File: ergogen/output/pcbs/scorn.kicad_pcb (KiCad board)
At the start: 2 copper layers, 150.5 x 92.9 mm, 46 parts

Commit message: pcb layout complete
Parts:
- removed B1: , E73:SW_TACT_ALPS_SKQGABE010
- removed OLED1: OLED, lib:OLED_headers
- removed S1, S10, S11, S12, S13, S14, S15, S16, S17, S18, S19, S2, S20, S21, S3, S4, S5, S6, S7, S8, S9: , PG1350
- added D22: , ceoloide:diode_tht_sod123, B.Cu at (141.0, 149.8)
- added D23: , ceoloide:diode_tht_sod123, B.Cu at (137.6, 133.1)
- added D24: , ceoloide:diode_tht_sod123, B.Cu at (134.3, 116.4)
- added D25: , ceoloide:diode_tht_sod123, B.Cu at (159.3, 146.6)
- added D26: , ceoloide:diode_tht_sod123, B.Cu at (157.7, 129.7)
- added D27: , ceoloide:diode_tht_sod123, B.Cu at (156.0, 112.7)
- added D28: , ceoloide:diode_tht_sod123, B.Cu at (177.1, 133.3)
- added D29: , ceoloide:diode_tht_sod123, B.Cu at (177.1, 116.3)
- added D30: , ceoloide:diode_tht_sod123, B.Cu at (177.1, 99.3)
- added D31: , ceoloide:diode_tht_sod123, B.Cu at (195.1, 128.3)
- added D32: , ceoloide:diode_tht_sod123, B.Cu at (195.1, 111.3)
- added D33: , ceoloide:diode_tht_sod123, B.Cu at (195.1, 94.3)
- added D34: , ceoloide:diode_tht_sod123, B.Cu at (213.1, 133.3)
- added D35: , ceoloide:diode_tht_sod123, B.Cu at (213.1, 116.3)
- added D36: , ceoloide:diode_tht_sod123, B.Cu at (213.1, 99.3)
- added D37: , ceoloide:diode_tht_sod123, B.Cu at (231.1, 135.3)
- added D38: , ceoloide:diode_tht_sod123, B.Cu at (231.1, 118.3)
- added D39: , ceoloide:diode_tht_sod123, B.Cu at (231.1, 101.3)
- added D40: , ceoloide:diode_tht_sod123, B.Cu at (210.0, 159.5)
- added D41: , ceoloide:diode_tht_sod123, B.Cu at (233.2, 158.1)
- added D42: , ceoloide:diode_tht_sod123, B.Cu at (256.9, 161.4)
- added DISP1: , ceoloide:display_ssd1306, F.Cu at (270.0, 114.8)
- added LED1: , ceoloide:led_SK6812mini-e (per-key, reversible), B.Cu at (148.4, 145.5)
- added LED10: , ceoloide:led_SK6812mini-e (per-key, reversible), B.Cu at (203.0, 125.1)
- added LED11: , ceoloide:led_SK6812mini-e (per-key, reversible), B.Cu at (203.0, 108.1)
- added LED12: , ceoloide:led_SK6812mini-e (per-key, reversible), B.Cu at (203.0, 91.1)
- added LED13: , ceoloide:led_SK6812mini-e (per-key, reversible), B.Cu at (221.0, 130.1)
- added LED14: , ceoloide:led_SK6812mini-e (per-key, reversible), B.Cu at (221.0, 113.1)
- added LED15: , ceoloide:led_SK6812mini-e (per-key, reversible), B.Cu at (221.0, 96.1)
- added LED16: , ceoloide:led_SK6812mini-e (per-key, reversible), B.Cu at (239.0, 132.1)
- added LED17: , ceoloide:led_SK6812mini-e (per-key, reversible), B.Cu at (239.0, 115.1)
- added LED18: , ceoloide:led_SK6812mini-e (per-key, reversible), B.Cu at (239.0, 98.1)
- added LED19: , ceoloide:led_SK6812mini-e (per-key, reversible), B.Cu at (217.6, 155.6)
- added LED2: , ceoloide:led_SK6812mini-e (per-key, reversible), B.Cu at (145.0, 128.8)
- added LED20: , ceoloide:led_SK6812mini-e (per-key, reversible), B.Cu at (241.4, 155.6)
- added LED21: , ceoloide:led_SK6812mini-e (per-key, reversible), B.Cu at (265.4, 160.8)
- added LED3: , ceoloide:led_SK6812mini-e (per-key, reversible), B.Cu at (141.6, 112.1)
- added LED4: , ceoloide:led_SK6812mini-e (per-key, reversible), B.Cu at (167.0, 142.8)
- added LED5: , ceoloide:led_SK6812mini-e (per-key, reversible), B.Cu at (165.3, 125.9)
- added LED6: , ceoloide:led_SK6812mini-e (per-key, reversible), B.Cu at (163.6, 109.0)
- added LED7: , ceoloide:led_SK6812mini-e (per-key, reversible), B.Cu at (185.0, 130.1)
- added LED8: , ceoloide:led_SK6812mini-e (per-key, reversible), B.Cu at (185.0, 113.1)
- added LED9: , ceoloide:led_SK6812mini-e (per-key, reversible), B.Cu at (185.0, 96.1)
- added MH1: , ceoloide:mounting_hole_npth, F.Cu at (154.4, 124.1)
- added MH2: , ceoloide:mounting_hole_npth, F.Cu at (157.3, 140.9)
- added MH3: , ceoloide:mounting_hole_npth, F.Cu at (255.0, 97.8)
- added MH4: , ceoloide:mounting_hole_npth, F.Cu at (275.9, 157.6)
- added MH5: , ceoloide:mounting_hole_npth, F.Cu at (203.2, 163.6)
- added RST1: , ceoloide:reset_switch_tht_top, F.Cu at (278.0, 135.8)
- added SW1: , ceoloide:switch_choc_v1_v2, B.Cu at (149.0, 150.1)
- added SW10: , ceoloide:switch_choc_v1_v2, B.Cu at (203.0, 129.8)
- added SW11: , ceoloide:switch_choc_v1_v2, B.Cu at (203.0, 112.8)
- added SW12: , ceoloide:switch_choc_v1_v2, B.Cu at (203.0, 95.8)
- added SW13: , ceoloide:switch_choc_v1_v2, B.Cu at (221.0, 134.8)
- added SW14: , ceoloide:switch_choc_v1_v2, B.Cu at (221.0, 117.8)
- added SW15: , ceoloide:switch_choc_v1_v2, B.Cu at (221.0, 100.8)
- added SW16: , ceoloide:switch_choc_v1_v2, B.Cu at (239.0, 136.8)
- added SW17: , ceoloide:switch_choc_v1_v2, B.Cu at (239.0, 119.8)
- added SW18: , ceoloide:switch_choc_v1_v2, B.Cu at (239.0, 102.8)
- added SW19: , ceoloide:switch_choc_v1_v2, B.Cu at (218.0, 160.3)
- added SW2: , ceoloide:switch_choc_v1_v2, B.Cu at (145.7, 133.4)
- added SW20: , ceoloide:switch_choc_v1_v2, B.Cu at (241.0, 160.3)
- added SW21: , ceoloide:switch_choc_v1_v2, B.Cu at (264.0, 165.3)
- added SW3: , ceoloide:switch_choc_v1_v2, B.Cu at (142.3, 116.7)
- added SW4: , ceoloide:switch_choc_v1_v2, B.Cu at (167.3, 147.5)
- added SW5: , ceoloide:switch_choc_v1_v2, B.Cu at (165.6, 130.6)
- added SW6: , ceoloide:switch_choc_v1_v2, B.Cu at (164.0, 113.7)
- added SW7: , ceoloide:switch_choc_v1_v2, B.Cu at (185.0, 134.8)
- added SW8: , ceoloide:switch_choc_v1_v2, B.Cu at (185.0, 117.8)
- added SW9: , ceoloide:switch_choc_v1_v2, B.Cu at (185.0, 100.8)
- D1, D10, D11, D12, D13, D14, D15, D16, D17, D18, D19, D2, D20, D21, D3, D4, D5, D6, D7, D8, D9: footprint ComboDiode -> ceoloide:diode_tht_sod123
- MCU1: footprint ProMicro -> ceoloide:mcu_nice_nano
- TRRS1: value TRRS-PJ-320A-dual -> (none); footprint TRRS-PJ-320A-dual -> ceoloide:trrs_pj320a (reversible, symmetric)
- moved D21 10.2 mm to (272.0, 166.3), turned to -108 degrees
- moved D4 10.2 mm to (175.1, 145.5), turned to -86 degrees
- moved D5 10.2 mm to (173.4, 128.6), turned to -86 degrees
- moved D6 10.2 mm to (171.7, 111.6), turned to -86 degrees
- moved D19 10.2 mm to (225.7, 158.1), turned to -85 degrees
- moved D10 10.2 mm to (210.9, 128.3), turned to -90 degrees
- moved D11 10.2 mm to (210.9, 111.3), turned to -90 degrees
- moved D12 10.2 mm to (210.9, 94.3), turned to -90 degrees
- moved D13 10.2 mm to (228.9, 133.3), turned to -90 degrees
- moved D14 10.2 mm to (228.9, 116.3), turned to -90 degrees
- moved D15 10.2 mm to (228.9, 99.3), turned to -90 degrees
- moved D16 10.2 mm to (246.9, 135.3), turned to -90 degrees
- moved D17 10.2 mm to (246.9, 118.3), turned to -90 degrees
- moved D18 10.2 mm to (246.9, 101.3), turned to -90 degrees
- moved D7 10.2 mm to (192.9, 133.3), turned to -90 degrees
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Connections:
- net P1 renamed MCU1_13
- net P14 renamed MCU1_10
- net P15 renamed MCU1_9
- net P18 renamed MCU1_8
- net P19 renamed MCU1_7
- net P20 renamed MCU1_6
- net P21 renamed MCU1_5
- net P4 renamed MCU1_19
- net P5 renamed MCU1_20
- net P6 renamed MCU1_21
- net P7 renamed MCU1_22
- net P8 renamed MCU1_23
- D1 pad 1: (no net) -> R2
- D10 pad 1: (no net) -> R2
- D11 pad 1: (no net) -> R1
- D12 pad 1: (no net) -> R0
- D13 pad 1: (no net) -> R2
- D14 pad 1: (no net) -> R1
- D15 pad 1: (no net) -> R0
- D16 pad 1: (no net) -> R2
- D17 pad 1: (no net) -> R1
- D18 pad 1: (no net) -> R0
- D19 pad 1: (no net) -> R3
- D2 pad 1: (no net) -> R1
- D20 pad 1: (no net) -> R3
- D21 pad 1: (no net) -> R3
- D3 pad 1: (no net) -> R0
- D4 pad 1: (no net) -> R2
- D5 pad 1: (no net) -> R1
- D6 pad 1: (no net) -> R0
- D7 pad 1: (no net) -> R2
- D8 pad 1: (no net) -> R1
- D9 pad 1: (no net) -> R0
- MCU1 pad 1: RAW -> MCU1_1
- MCU1 pad 11: P16 -> MCU1_11
- MCU1 pad 12: P10 -> MCU1_12
- MCU1 pad 14: P0 -> MCU1_14
- MCU1 pad 15: GND -> MCU1_15
- MCU1 pad 16: GND -> MCU1_16
- MCU1 pad 17: P2 -> MCU1_17
- MCU1 pad 18: P3 -> MCU1_18
- MCU1 pad 2: GND -> MCU1_2
- MCU1 pad 24: P9 -> MCU1_24
- MCU1 pad 3: RST -> MCU1_3
- MCU1 pad 4: VCC -> MCU1_4
- TRRS1 pad 3: P9 -> DAT
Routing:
- net (no net): track 0.00 -> 337.7 mm
- net VCC: track 0.00 -> 82.3 mm, vias 0 -> 21
- net GND: track 0.00 -> 82.3 mm, vias 0 -> 21
- net LED_20: track 0.00 -> 13.5 mm, vias 0 -> 2
- net LED_18: track 0.00 -> 13.5 mm, vias 0 -> 2
- net LED_16: track 0.00 -> 13.5 mm, vias 0 -> 2
- net LED_4: track 0.00 -> 13.5 mm, vias 0 -> 2
- net LED_13: track 0.00 -> 13.5 mm, vias 0 -> 2
- net LED_15: track 0.00 -> 13.5 mm, vias 0 -> 2
- net LED_14: track 0.00 -> 13.5 mm, vias 0 -> 2
- net LED_12: track 0.00 -> 13.5 mm, vias 0 -> 2
- net LED_9: track 0.00 -> 13.5 mm, vias 0 -> 2
- net LED_3: track 0.00 -> 13.5 mm, vias 0 -> 2
- net LED_2: track 0.00 -> 13.5 mm, vias 0 -> 2
- net LED_11: track 0.00 -> 13.5 mm, vias 0 -> 2
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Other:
- board text added: "JLCJLCJLCJLC"

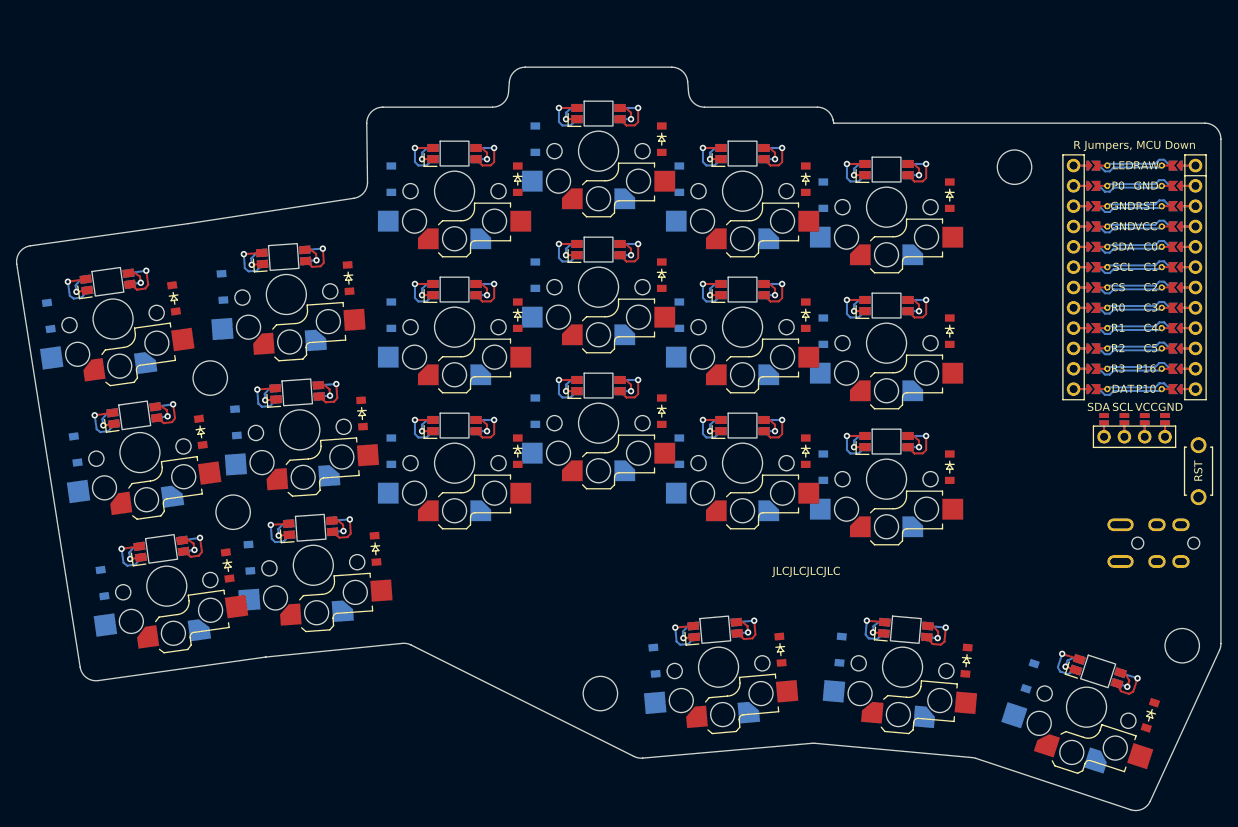
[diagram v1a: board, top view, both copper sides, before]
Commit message: stagger and splay rework
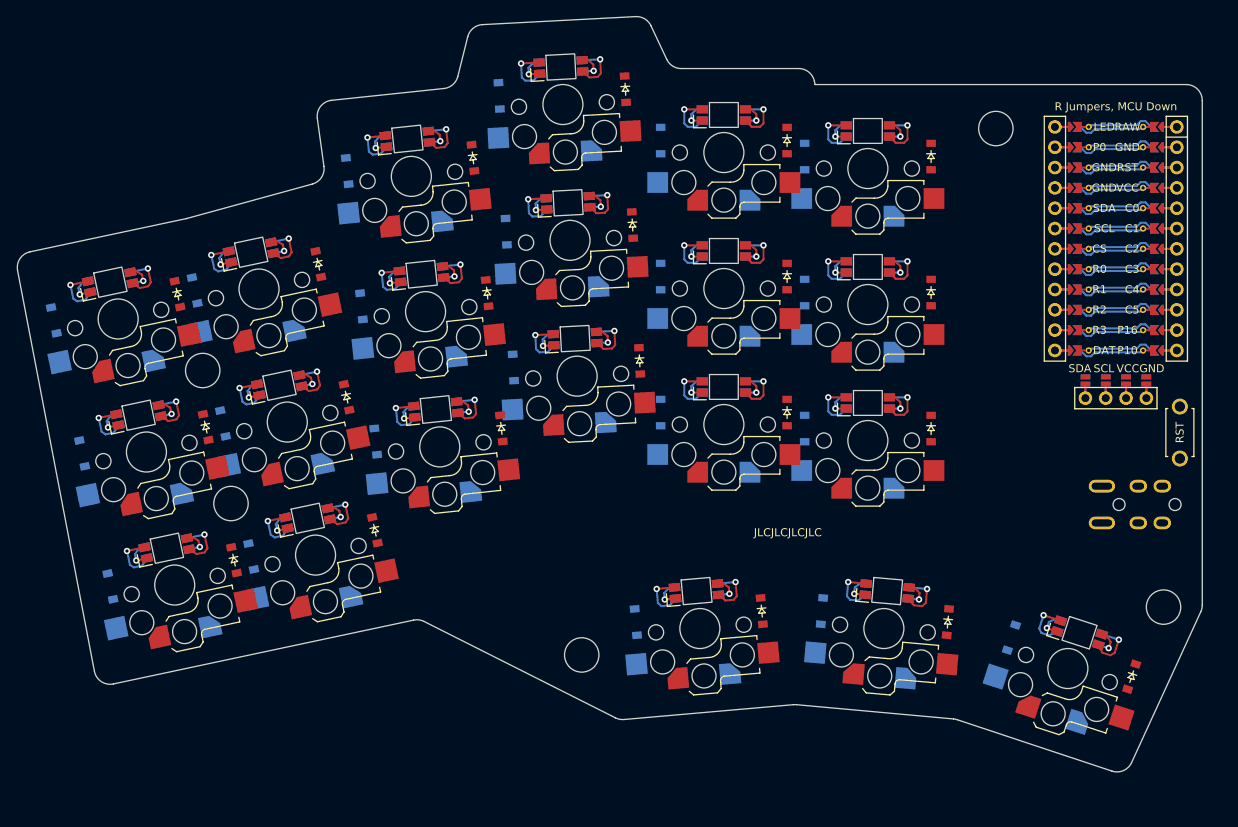
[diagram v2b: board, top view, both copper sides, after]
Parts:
- moved D12 7.72 mm to (206.3, 88.0), turned to -87 degrees
- moved LED12 7.48 mm to (198.3, 85.2), turned to 3 degrees
- moved SW12 7.34 mm to (198.5, 89.9), turned to 183 degrees
- moved D11 7.25 mm to (207.2, 105.0), turned to -87 degrees
- moved D33 7.05 mm to (190.6, 88.9), turned to -87 degrees
- moved LED11 6.98 mm to (199.2, 102.2), turned to 3 degrees
- moved D10 6.87 mm to (208.1, 122.0), turned to -87 degrees
- moved SW11 6.85 mm to (199.4, 106.9), turned to 183 degrees
- moved LED10 6.56 mm to (200.1, 119.2), turned to 3 degrees
- moved D32 6.54 mm to (191.4, 105.8), turned to -87 degrees
- moved SW10 6.46 mm to (200.3, 123.9), turned to 183 degrees
- moved D9 6.20 mm to (187.3, 96.6), turned to -84 degrees
- moved LED9 6.17 mm to (179.1, 94.2), turned to 6 degrees
- moved D31 6.11 mm to (192.3, 122.8), turned to -87 degrees
- moved SW9 5.71 mm to (179.6, 98.9), turned to 186 degrees
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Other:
- board size 150.5 x 92.9 mm -> 148.1 x 94.4 mm
